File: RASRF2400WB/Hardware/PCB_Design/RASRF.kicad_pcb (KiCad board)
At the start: 4 copper layers, 76.6 x 57 mm, 176 parts, among them J1 PCIexpress_x8, J3 60312202111527, J4 Conn_01x04_Pin, U1 LD1117S18TR_SOT223, U2 STM32C031G6Ux, U3 SN74AXC4T774RSVR, U4 TCR2EF285, U5 MAX2831ETM+T, U6 HHM1902B1, U7 ADC3221IRGZR, Y1 7L-40.000MBS-T, Y2 ABM10-166-12.000MHZ-T3

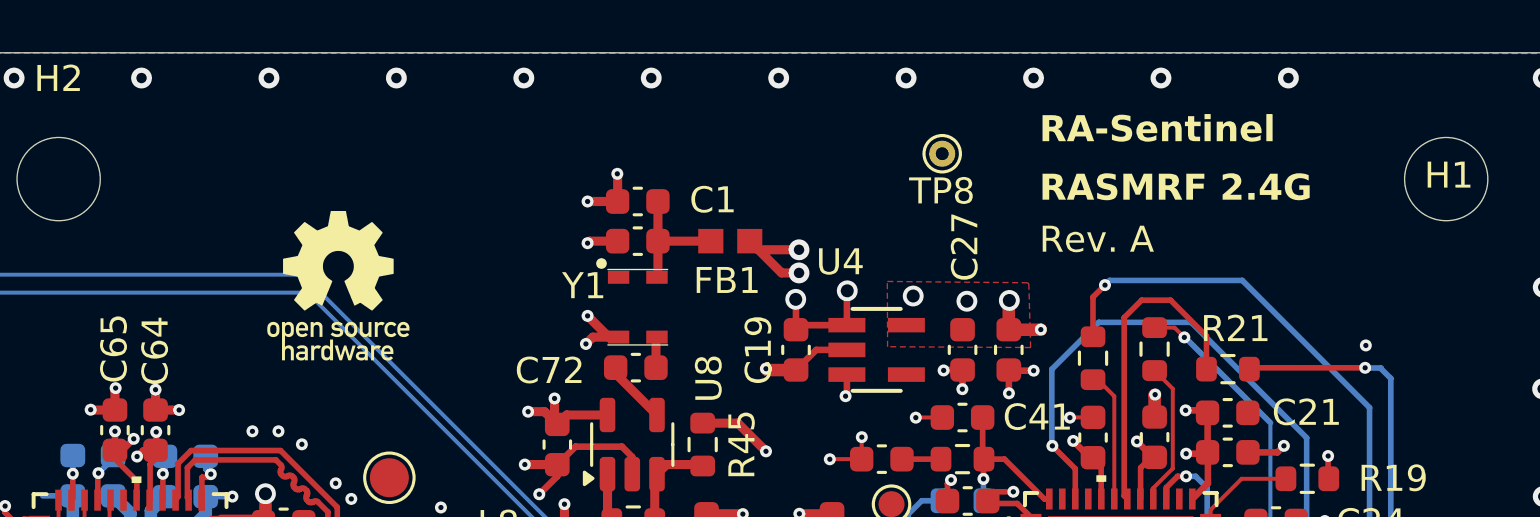
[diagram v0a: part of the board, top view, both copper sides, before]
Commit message: added license note on silkscreen removed older RASBB revision
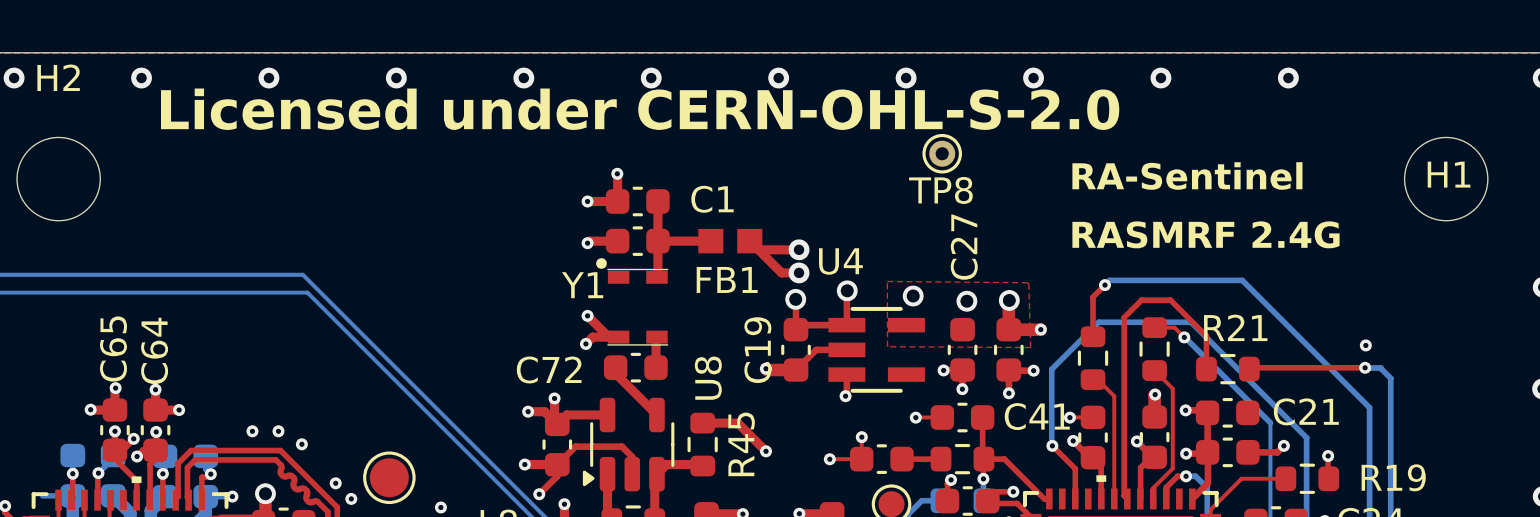
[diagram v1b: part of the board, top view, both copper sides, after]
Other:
- board text added: "Licensed under CERN-OHL-S-2.0"
- board text removed: "Rev. A"
